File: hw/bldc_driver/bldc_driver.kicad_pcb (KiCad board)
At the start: 2 copper layers, 13 parts, among them Q1 Q_NMOS_DGS, U1 CH32V30xRxTx, U2 STGAP2SCM, U3 STGAP2SCM, U4 STGAP2SCM, U5 STGAP2SCM, U6 STGAP2SCM, U7 STGAP2SCM

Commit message: feat: add CNCs
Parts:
- added C11: 0.1 µF, Capacitor_SMD:C_0805_2012Metric_Pad1.18x1.45mm_HandSolder, F.Cu at (114.5, 88.9)
- added C13: 0.1 µF, Capacitor_SMD:C_0805_2012Metric_Pad1.18x1.45mm_HandSolder, F.Cu at (114.5, 91.9)
- added C15: 0.1 µF, Capacitor_SMD:C_0805_2012Metric_Pad1.18x1.45mm_HandSolder, F.Cu at (114.5, 94.9)
- added C16: 10 µF, Capacitor_SMD:C_0805_2012Metric_Pad1.18x1.45mm_HandSolder, F.Cu at (114.5, 97.9)
- added C17: 0.1 µF, Capacitor_SMD:C_0805_2012Metric_Pad1.18x1.45mm_HandSolder, F.Cu at (114.5, 100.9)
- added C18: 0.1 µF, Capacitor_SMD:C_0805_2012Metric_Pad1.18x1.45mm_HandSolder, F.Cu at (114.5, 103.9)
- added C19: 22 µF, Capacitor_SMD:C_0805_2012Metric_Pad1.18x1.45mm_HandSolder, F.Cu at (114.5, 107.0)
- added C20: 22 µF, Capacitor_SMD:C_0805_2012Metric_Pad1.18x1.45mm_HandSolder, F.Cu at (114.5, 110.0)
- added C21: 0.1 µF, Capacitor_SMD:C_0805_2012Metric_Pad1.18x1.45mm_HandSolder, F.Cu at (119.3, 88.9)
- added C22: 0.1 µF, Capacitor_SMD:C_0805_2012Metric_Pad1.18x1.45mm_HandSolder, F.Cu at (119.3, 91.9)
- added C23: 330 pF, Capacitor_SMD:C_0805_2012Metric_Pad1.18x1.45mm_HandSolder, F.Cu at (119.3, 94.9)
- added C24: 330 pF, Capacitor_SMD:C_0805_2012Metric_Pad1.18x1.45mm_HandSolder, F.Cu at (119.3, 97.9)
- added C25: 0.1 µF, Capacitor_SMD:C_0805_2012Metric_Pad1.18x1.45mm_HandSolder, F.Cu at (119.3, 100.9)
- added C26: 0.1 µF, Capacitor_SMD:C_0805_2012Metric_Pad1.18x1.45mm_HandSolder, F.Cu at (119.3, 103.9)
- added C27: 330 pF, Capacitor_SMD:C_0805_2012Metric_Pad1.18x1.45mm_HandSolder, F.Cu at (119.3, 107.0)
- added C28: 0.1 µF, Capacitor_SMD:C_0805_2012Metric_Pad1.18x1.45mm_HandSolder, F.Cu at (119.3, 110.0)
- added C29: 0.1 µF, Capacitor_SMD:C_0805_2012Metric_Pad1.18x1.45mm_HandSolder, F.Cu at (124.2, 88.9)
- added C30: 330 pF, Capacitor_SMD:C_0805_2012Metric_Pad1.18x1.45mm_HandSolder, F.Cu at (124.2, 91.9)
- added C31: 0.1 µF, Capacitor_SMD:C_0805_2012Metric_Pad1.18x1.45mm_HandSolder, F.Cu at (124.2, 94.9)
- added C32: 0.1 µF, Capacitor_SMD:C_0805_2012Metric_Pad1.18x1.45mm_HandSolder, F.Cu at (124.2, 97.9)
- added C34: 0.1 µF, Capacitor_SMD:C_0805_2012Metric_Pad1.18x1.45mm_HandSolder, F.Cu at (124.2, 100.9)
- added C36: 0.1 µF, Capacitor_SMD:C_0805_2012Metric_Pad1.18x1.45mm_HandSolder, F.Cu at (124.2, 103.9)
- added C38: 0.1 µF, Capacitor_SMD:C_0805_2012Metric_Pad1.18x1.45mm_HandSolder, F.Cu at (124.2, 107.0)
- added C39: 0.1 µF, Capacitor_SMD:C_0805_2012Metric_Pad1.18x1.45mm_HandSolder, F.Cu at (177.0, 96.0)
- added C44: 0.1 µF, Capacitor_SMD:C_0805_2012Metric_Pad1.18x1.45mm_HandSolder, F.Cu at (124.2, 110.0)
- added C46: 0.1 µF, Capacitor_SMD:C_0805_2012Metric_Pad1.18x1.45mm_HandSolder, F.Cu at (129.0, 88.9)
- added C48: 0.1 µF, Capacitor_SMD:C_0805_2012Metric_Pad1.18x1.45mm_HandSolder, F.Cu at (129.0, 91.9)
- added C5: 10 µF, Capacitor_SMD:C_0805_2012Metric_Pad1.18x1.45mm_HandSolder, F.Cu at (177.0, 80.9)
- added C50: 0.1 µF, Capacitor_SMD:C_0805_2012Metric_Pad1.18x1.45mm_HandSolder, F.Cu at (129.0, 94.9)
- added C52: 0.1 µF, Capacitor_SMD:C_0805_2012Metric_Pad1.18x1.45mm_HandSolder, F.Cu at (129.0, 97.9)
- added C54: 0.1 µF, Capacitor_SMD:C_0805_2012Metric_Pad1.18x1.45mm_HandSolder, F.Cu at (129.0, 100.9)
- added C6: 0.1 µF, Capacitor_SMD:C_0805_2012Metric_Pad1.18x1.45mm_HandSolder, F.Cu at (177.0, 83.9)
- added C7: 0.1 µF, Capacitor_SMD:C_0805_2012Metric_Pad1.18x1.45mm_HandSolder, F.Cu at (177.0, 87.0)
- added C8: 22 µF, Capacitor_SMD:C_0805_2012Metric_Pad1.18x1.45mm_HandSolder, F.Cu at (177.0, 90.0)
- added C9: 22 µF, Capacitor_SMD:C_0805_2012Metric_Pad1.18x1.45mm_HandSolder, F.Cu at (177.0, 93.0)
- added D1: KT-0603W, LED_SMD:LED_0603_1608Metric_Pad1.05x0.95mm_HandSolder, F.Cu at (171.7, 92.8)
- added D10: 1N4148WS, Diode_SMD:D_SOD-323_HandSoldering, F.Cu at (151.3, 91.8)
- added D11: 1N4148WS, Diode_SMD:D_SOD-323_HandSoldering, F.Cu at (151.3, 94.8)
- added D12: 1N4148WS, Diode_SMD:D_SOD-323_HandSoldering, F.Cu at (151.3, 97.7)
- added D13: 1N4148WS, Diode_SMD:D_SOD-323_HandSoldering, F.Cu at (151.3, 100.7)
- added D14: 1N4148WS, Diode_SMD:D_SOD-323_HandSoldering, F.Cu at (151.3, 103.6)
- added D15: KT-0603W, LED_SMD:LED_0603_1608Metric_Pad1.05x0.95mm_HandSolder, F.Cu at (171.7, 95.4)
- added D16: KT-0603W, LED_SMD:LED_0603_1608Metric_Pad1.05x0.95mm_HandSolder, F.Cu at (171.7, 98.0)
- added D17: KT-0603W, LED_SMD:LED_0603_1608Metric_Pad1.05x0.95mm_HandSolder, F.Cu at (171.7, 100.6)
- added D2: PESD15VL1BA, Diode_SMD:D_SOD-323_HandSoldering, F.Cu at (187.3, 77.5)
- added D3: MBR20100DT, Package_TO_SOT_SMD:TO-252-2, F.Cu at (92.9, 91.6)
- added D4: MBR20100DT, Package_TO_SOT_SMD:TO-252-2, F.Cu at (92.9, 99.8)
- added D5: MBR20100DT, Package_TO_SOT_SMD:TO-252-2, F.Cu at (92.9, 108.0)
- added D6: MBR20100DT, Package_TO_SOT_SMD:TO-252-2, F.Cu at (92.9, 116.1)
- added D7: MBR20100DT, Package_TO_SOT_SMD:TO-252-2, F.Cu at (92.9, 124.3)
- added D8: MBR20100DT, Package_TO_SOT_SMD:TO-252-2, F.Cu at (92.9, 132.5)
- added D9: 1N4148WS, Diode_SMD:D_SOD-323_HandSoldering, F.Cu at (151.3, 88.9)
- added FL1: BNX025, Filter:Filter_Murata_BNX025, F.Cu at (166.8, 72.4)
- added J1: 430450412, Connector_Molex:Molex_Micro-Fit_3.0_43045-0412_2x02_P3.00mm_Vertical, F.Cu at (161.9, 95.0)
- added J2: B4B-EH-A(LF)(SN), Connector_JST:JST_EH_B4B-EH-A_1x04_P2.50mm_Vertical, F.Cu at (179.8, 68.0)
- added J4: 1733583, TerminalBlock_Phoenix:TerminalBlock_Phoenix_MKDS-1,5-3-5.08_1x03_P5.08mm_Horizontal, F.Cu at (160.8, 85.7)
- added L1: KOHER_MDA7030 15uH, Inductor_SMD:L_KOHERelec_MDA7030, F.Cu at (184.2, 97.5)
- added L2: KOHER_MDA7030 15uH, Inductor_SMD:L_KOHERelec_MDA7030, F.Cu at (116.9, 115.6)
- added Q1: IRF540N, Package_TO_SOT_THT:TO-220-3_Horizontal_TabDown, F.Cu at (89.2, 85.6)
- added Q2: IRF540N, Package_TO_SOT_THT:TO-220-3_Horizontal_TabDown, F.Cu at (100.8, 85.6)
- added Q3: IRF540N, Package_TO_SOT_THT:TO-220-3_Horizontal_TabDown, F.Cu at (112.3, 85.6)
- added Q4: IRF540N, Package_TO_SOT_THT:TO-220-3_Horizontal_TabDown, F.Cu at (123.8, 85.6)
- added Q5: IRF540N, Package_TO_SOT_THT:TO-220-3_Horizontal_TabDown, F.Cu at (135.4, 85.6)
- added Q6: IRF540N, Package_TO_SOT_THT:TO-220-3_Horizontal_TabDown, F.Cu at (146.9, 85.6)
- added R10: 12 ohm, Resistor_SMD:R_0603_1608Metric_Pad0.98x0.95mm_HandSolder, F.Cu at (133.5, 93.7)
- added R11: 12 ohm, Resistor_SMD:R_0603_1608Metric_Pad0.98x0.95mm_HandSolder, F.Cu at (133.5, 96.2)
- added R12: 12 ohm, Resistor_SMD:R_0603_1608Metric_Pad0.98x0.95mm_HandSolder, F.Cu at (133.5, 98.7)
- added R13: 12 ohm, Resistor_SMD:R_0603_1608Metric_Pad0.98x0.95mm_HandSolder, F.Cu at (133.5, 101.2)
- added R14: 12 ohm, Resistor_SMD:R_0603_1608Metric_Pad0.98x0.95mm_HandSolder, F.Cu at (133.5, 103.7)
- added R15: 12 ohm, Resistor_SMD:R_0603_1608Metric_Pad0.98x0.95mm_HandSolder, F.Cu at (133.5, 106.2)
- added R16: 12 ohm, Resistor_SMD:R_0603_1608Metric_Pad0.98x0.95mm_HandSolder, F.Cu at (137.9, 88.6)
- added R17: 12 ohm, Resistor_SMD:R_0603_1608Metric_Pad0.98x0.95mm_HandSolder, F.Cu at (137.9, 91.2)
- added R18: 470 kohm, Resistor_SMD:R_0603_1608Metric_Pad0.98x0.95mm_HandSolder, F.Cu at (137.9, 93.7)
- added R19: 10 kohm, Resistor_SMD:R_0603_1608Metric_Pad0.98x0.95mm_HandSolder, F.Cu at (137.9, 96.2)
- added R2: 100 Ohm, Resistor_SMD:R_0603_1608Metric_Pad0.98x0.95mm_HandSolder, F.Cu at (186.2, 80.7)
- added R20: 470 kohm, Resistor_SMD:R_0603_1608Metric_Pad0.98x0.95mm_HandSolder, F.Cu at (137.9, 98.7)
- added R21: 10 kohm, Resistor_SMD:R_0603_1608Metric_Pad0.98x0.95mm_HandSolder, F.Cu at (137.9, 101.2)
- added R22: 470 kohm, Resistor_SMD:R_0603_1608Metric_Pad0.98x0.95mm_HandSolder, F.Cu at (137.9, 103.7)
- added R23: 10 kohm, Resistor_SMD:R_0603_1608Metric_Pad0.98x0.95mm_HandSolder, F.Cu at (137.9, 106.2)
- added R24: 12 ohm, Resistor_SMD:R_0603_1608Metric_Pad0.98x0.95mm_HandSolder, F.Cu at (142.2, 88.6)
- added R25: 12 ohm, Resistor_SMD:R_0603_1608Metric_Pad0.98x0.95mm_HandSolder, F.Cu at (142.2, 91.2)
- added R26: 12 ohm, Resistor_SMD:R_0603_1608Metric_Pad0.98x0.95mm_HandSolder, F.Cu at (142.2, 93.7)
- added R27: 12 ohm, Resistor_SMD:R_0603_1608Metric_Pad0.98x0.95mm_HandSolder, F.Cu at (142.2, 96.2)
- added R28: 12 ohm, Resistor_SMD:R_0603_1608Metric_Pad0.98x0.95mm_HandSolder, F.Cu at (142.2, 98.7)
- added R29: 12 ohm, Resistor_SMD:R_0603_1608Metric_Pad0.98x0.95mm_HandSolder, F.Cu at (142.2, 101.2)
- added R3: 0 ohm, Resistor_SMD:R_0201_0603Metric_Pad0.64x0.40mm_HandSolder, F.Cu at (176.0, 98.4)
- added R30: 12 ohm, Resistor_SMD:R_0603_1608Metric_Pad0.98x0.95mm_HandSolder, F.Cu at (142.2, 103.7)
- added R31: 12 ohm, Resistor_SMD:R_0603_1608Metric_Pad0.98x0.95mm_HandSolder, F.Cu at (142.2, 106.2)
- added R32: 12 ohm, Resistor_SMD:R_0603_1608Metric_Pad0.98x0.95mm_HandSolder, F.Cu at (146.6, 88.6)
- added R33: 12 ohm, Resistor_SMD:R_0603_1608Metric_Pad0.98x0.95mm_HandSolder, F.Cu at (146.6, 91.2)
- added R34: 12 ohm, Resistor_SMD:R_0603_1608Metric_Pad0.98x0.95mm_HandSolder, F.Cu at (146.6, 93.7)
- added R35: 12 ohm, Resistor_SMD:R_0603_1608Metric_Pad0.98x0.95mm_HandSolder, F.Cu at (146.6, 96.2)
- added R36: 100 Ohm, Resistor_SMD:R_0603_1608Metric_Pad0.98x0.95mm_HandSolder, F.Cu at (186.2, 88.2)
- added R37: 100 Ohm, Resistor_SMD:R_0603_1608Metric_Pad0.98x0.95mm_HandSolder, F.Cu at (186.2, 90.7)
- added R4: 100 kohm, Resistor_SMD:R_0201_0603Metric_Pad0.64x0.40mm_HandSolder, F.Cu at (176.0, 100.1)
- added R5: 22 kohm, Resistor_SMD:R_0603_1608Metric_Pad0.98x0.95mm_HandSolder, F.Cu at (186.2, 83.2)
- added R6: 100 Ohm, Resistor_SMD:R_0603_1608Metric_Pad0.98x0.95mm_HandSolder, F.Cu at (186.2, 85.7)
- added R7: 0 ohm, Resistor_SMD:R_0201_0603Metric_Pad0.64x0.40mm_HandSolder, F.Cu at (113.5, 134.7)
- added R8: 200 kohm, Resistor_SMD:R_0603_1608Metric_Pad0.98x0.95mm_HandSolder, F.Cu at (133.5, 88.6)
- added R9: 27 kohm, Resistor_SMD:R_0603_1608Metric_Pad0.98x0.95mm_HandSolder, F.Cu at (133.5, 91.2)
- added TP1: TestPoint_Flag, TestPoint:TestPoint_Plated_Hole_D2.0mm, F.Cu at (181.7, 81.8)
- added TP2: TestPoint_Flag, TestPoint:TestPoint_Plated_Hole_D2.0mm, F.Cu at (181.7, 86.4)
- added TP3: TestPoint_Flag, TestPoint:TestPoint_Plated_Hole_D2.0mm, F.Cu at (181.7, 91.1)
- added TP4: TestPoint_Flag, TestPoint:TestPoint_Plated_Hole_D2.0mm, F.Cu at (114.5, 122.0)
- added TP5: TestPoint_Flag, TestPoint:TestPoint_Plated_Hole_D2.0mm, F.Cu at (114.5, 126.7)
- added U10: TPS54202DDC, Package_TO_SOT_SMD:SOT-23-6_Handsoldering, F.Cu at (115.0, 131.5)
- added U11: AMC1200BDWV, Package_SO:SOIC-8_7.5x5.85mm_P1.27mm, F.Cu at (105.1, 98.5)
- added U12: AMC1200BDWV, Package_SO:SOIC-8_7.5x5.85mm_P1.27mm, F.Cu at (105.1, 105.9)
- added U13: AMC1200BDWV, Package_SO:SOIC-8_7.5x5.85mm_P1.27mm, F.Cu at (105.1, 113.3)
- added U14: SN65HVD230, Package_SO:SOIC-8_3.9x4.9mm_P1.27mm, F.Cu at (180.5, 74.6)
- added U8: TPS54202DDC, Package_TO_SOT_SMD:SOT-23-6_Handsoldering, F.Cu at (187.7, 73.7)
- added U9: AMC1200BDWV, Package_SO:SOIC-8_7.5x5.85mm_P1.27mm, F.Cu at (105.1, 91.1)
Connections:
- U1 pad 10: /Motor/PH_V_HI -> /Motor/W_ADC_P
- U1 pad 11: /Motor/PH_V_LO -> /Motor/SHUNT_CURR_P
- U1 pad 24: /Motor/PH_W_HI -> unconnected-(U1-PC4-Pad24)
- U1 pad 25: /Motor/PH_W_LO -> unconnected-(U1-PC5-Pad25)
- U1 pad 34: unconnected-(U1-PB13-Pad34) -> Net-(D15-A)
- U1 pad 35: unconnected-(U1-PB14-Pad35) -> Net-(D16-A)
- U1 pad 36: unconnected-(U1-PB15-Pad36) -> Net-(D17-A)
- U1 pad 37: unconnected-(U1-PC6-Pad37) -> /Motor/PH_U_HI
- U1 pad 38: unconnected-(U1-PC7-Pad38) -> /Motor/PH_U_LO
- U1 pad 39: unconnected-(U1-PC8-Pad39) -> /Motor/PH_V_HI
- U1 pad 40: unconnected-(U1-PC9-Pad40) -> /Motor/PH_V_LO
- U1 pad 44: unconnected-(U1-PA11-Pad44) -> /CAN_RX
- U1 pad 45: unconnected-(U1-PA12-Pad45) -> /CAN_TX
- U1 pad 46: unconnected-(U1-SWDIO-Pad46) -> Net-(J2-Pin_3)
- U1 pad 49: unconnected-(U1-SWCLK-Pad49) -> Net-(J2-Pin_2)
- U1 pad 51: unconnected-(U1-PC10-Pad51) -> /Motor/PH_W_HI
- U1 pad 52: unconnected-(U1-PC11-Pad52) -> /Motor/PH_W_LO
- U1 pad 8: /Motor/PH_U_HI -> /Motor/U_ADC_P
- U1 pad 9: /Motor/PH_U_LO -> /Motor/V_ADC_P
- U2 pad 1: unconnected-(U2-VDD-Pad1) -> +3V3
- U2 pad 4: unconnected-(U2-GND-Pad4) -> GND
- U2 pad 5: unconnected-(U2-VH-Pad5) -> +VDC
- U2 pad 6: unconnected-(U2-GOUT-Pad6) -> Net-(D9-K)
- U2 pad 7: unconnected-(U2-CLAMP-Pad7) -> Net-(Q2-G)
- U2 pad 8: unconnected-(U2-GNDISO-Pad8) -> GNDPWR
- U3 pad 1: unconnected-(U3-VDD-Pad1) -> +3V3
- U3 pad 4: unconnected-(U3-GND-Pad4) -> GND
- U3 pad 5: unconnected-(U3-VH-Pad5) -> +VDC
- U3 pad 6: unconnected-(U3-GOUT-Pad6) -> Net-(D10-K)
- U3 pad 7: unconnected-(U3-CLAMP-Pad7) -> Net-(Q1-G)
- U3 pad 8: unconnected-(U3-GNDISO-Pad8) -> GNDPWR
- U4 pad 1: unconnected-(U4-VDD-Pad1) -> +3V3
- U4 pad 4: unconnected-(U4-GND-Pad4) -> GND
- U4 pad 5: unconnected-(U4-VH-Pad5) -> +VDC
- U4 pad 6: unconnected-(U4-GOUT-Pad6) -> Net-(D11-K)
- U4 pad 7: unconnected-(U4-CLAMP-Pad7) -> Net-(Q3-G)
- U4 pad 8: unconnected-(U4-GNDISO-Pad8) -> GNDPWR
- U5 pad 1: unconnected-(U5-VDD-Pad1) -> +3V3
- U5 pad 4: unconnected-(U5-GND-Pad4) -> GND
- U5 pad 5: unconnected-(U5-VH-Pad5) -> +VDC
- U5 pad 6: unconnected-(U5-GOUT-Pad6) -> Net-(D12-K)
- U5 pad 7: unconnected-(U5-CLAMP-Pad7) -> Net-(Q4-G)
- U5 pad 8: unconnected-(U5-GNDISO-Pad8) -> GNDPWR
- U6 pad 1: unconnected-(U6-VDD-Pad1) -> +3V3
- U6 pad 4: unconnected-(U6-GND-Pad4) -> GND
- U6 pad 5: unconnected-(U6-VH-Pad5) -> +VDC
- U6 pad 6: unconnected-(U6-GOUT-Pad6) -> Net-(D13-K)
- U6 pad 7: unconnected-(U6-CLAMP-Pad7) -> Net-(Q5-G)
- U6 pad 8: unconnected-(U6-GNDISO-Pad8) -> GNDPWR
- U7 pad 1: unconnected-(U7-VDD-Pad1) -> +3V3
- U7 pad 4: unconnected-(U7-GND-Pad4) -> GND
- U7 pad 5: unconnected-(U7-VH-Pad5) -> +VDC
- U7 pad 6: unconnected-(U7-GOUT-Pad6) -> Net-(D14-K)
- U7 pad 7: unconnected-(U7-CLAMP-Pad7) -> Net-(Q6-G)
- U7 pad 8: unconnected-(U7-GNDISO-Pad8) -> GNDPWR
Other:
- board outline added: 127.5 x 96 mm

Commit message: feat: start PCB
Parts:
- added F1: BSMD1206C-2200T, Fuse:Fuse_1206_3216Metric_Pad1.42x1.75mm_HandSolder, F.Cu at (155.9, 123.9)
- added J3: B4B-EH-A(LF)(SN), Connector_JST:JST_EH_B4B-EH-A_1x04_P2.50mm_Vertical, F.Cu at (156.5, 119.0)
- added TP6: TestPoint_Flag, TestPoint:TestPoint_Plated_Hole_D2.0mm, F.Cu at (150.7, 118.7)
- added TP7: TestPoint_Flag, TestPoint:TestPoint_Plated_Hole_D2.0mm, F.Cu at (150.7, 123.3)
- added TP8: TestPoint_Flag, TestPoint:TestPoint_Plated_Hole_D2.0mm, F.Cu at (150.7, 128.0)
- added TP9: TestPoint_Flag, TestPoint:TestPoint_Plated_Hole_D2.0mm, F.Cu at (150.7, 132.7)
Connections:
- J1 pad 1: +VDC -> Net-(J1-Pin_1)
- U1 pad 29: unconnected-(U1-PB10-Pad29) -> /USART3_TX
- U1 pad 30: unconnected-(U1-PB11-Pad30) -> /USART3_RX

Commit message: bldc: start placement
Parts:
- removed Q1: Q_NMOS_DGS, Package_TO_SOT_SMD:TO-252-2
- removed Q1: IRF540N, Package_TO_SOT_THT:TO-220-3_Horizontal_TabDown
- removed TP4: TestPoint_Flag, TestPoint:TestPoint_Plated_Hole_D2.0mm
- added C10: 1 µF, Capacitor_SMD:C_0805_2012Metric_Pad1.18x1.45mm_HandSolder, F.Cu at (139.7, 79.2)
- added C12: 1 µF, Capacitor_SMD:C_0805_2012Metric_Pad1.18x1.45mm_HandSolder, F.Cu at (89.0, 64.0)
- added C14: 1 µF, Capacitor_SMD:C_0805_2012Metric_Pad1.18x1.45mm_HandSolder, F.Cu at (89.0, 67.1)
- added C33: 1 µF, Capacitor_SMD:C_0805_2012Metric_Pad1.18x1.45mm_HandSolder, F.Cu at (89.0, 70.1)
- added C35: 1 µF, Capacitor_SMD:C_0805_2012Metric_Pad1.18x1.45mm_HandSolder, F.Cu at (93.8, 61.0)
- added C37: 1 µF, Capacitor_SMD:C_0805_2012Metric_Pad1.18x1.45mm_HandSolder, F.Cu at (93.8, 64.0)
- added C43: 1 µF, Capacitor_SMD:C_0805_2012Metric_Pad1.18x1.45mm_HandSolder, F.Cu at (93.8, 67.1)
- added C45: 1 µF, Capacitor_SMD:C_0805_2012Metric_Pad1.18x1.45mm_HandSolder, F.Cu at (93.8, 70.1)
- added C47: 1 µF, Capacitor_SMD:C_0805_2012Metric_Pad1.18x1.45mm_HandSolder, F.Cu at (98.6, 61.0)
- added C49: 1 µF, Capacitor_SMD:C_0805_2012Metric_Pad1.18x1.45mm_HandSolder, F.Cu at (98.6, 64.0)
- added C51: 1 µF, Capacitor_SMD:C_0805_2012Metric_Pad1.18x1.45mm_HandSolder, F.Cu at (98.6, 67.1)
- added C53: 1 µF, Capacitor_SMD:C_0805_2012Metric_Pad1.18x1.45mm_HandSolder, F.Cu at (98.6, 70.1)
- added Q7: IRF540N, Package_TO_SOT_THT:TO-220-3_Horizontal_TabDown, F.Cu at (109.3, 99.5)
- added Rshunt1: HoLLR2512-3W-15mR-1%, Resistor_SMD:R_2512_6332Metric_Pad1.40x3.35mm_HandSolder, B.Cu at (124.2, 96.6)
- C1, C11, C13, C15, C16, C17, C18, C2, C21, C22, C23, C24, C25, C26, C27, C28, C29, C3, C30, C31, C32, C34, C36, C38, C4, C44, C46, C48, C50, C52, C54, C6, C7, D3, D4, D5, D6, D7, D8, R10, R11, R12, R13, R14, R15, R16, R17, R18, R19, R20, R21, R22, R23, R24, R25, R26, R27, R28, R29, R30, R31, R32, R34, R35, R5, R9, U11, U9: moved to B.Cu
- moved TP9 93.0 mm to (73.5, 80.6), turned to 180 degrees
- moved TP8 87.3 mm to (77.3, 80.6)
- moved J4 83.3 mm to (77.5, 85.9), turned to -90 degrees
- moved TP7 81.7 mm to (81.0, 80.6)
- moved R35 76.1 mm to (79.5, 60.2), turned to 90 degrees
- moved R31 75.4 mm to (78.3, 66.3), turned to 90 degrees
- moved R34 72.7 mm to (82.0, 60.2), turned to 90 degrees
- moved R30 71.9 mm to (80.8, 66.3), turned to 90 degrees
- moved R23 69.4 mm to (78.3, 70.6), turned to 90 degrees
- moved R29 68.5 mm to (83.3, 66.3), turned to 90 degrees
- moved R32 67.6 mm to (85.3, 60.1), turned to 90 degrees
- moved R22 66.0 mm to (80.8, 70.6), turned to 90 degrees
- moved R28 65.0 mm to (85.9, 66.3), turned to 90 degrees
- moved U2 63.9 mm to (133.0, 82.6), turned to 180 degrees
- moved U4 62.9 mm to (133.0, 93.8), turned to 180 degrees
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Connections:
- net Net-(J2-Pin_2) renamed /SWCLK
- net Net-(J2-Pin_3) renamed /SWDIO
- J4 pad 1: /Motor/MOTOR_U -> /Motor/MOTOR_W
- J4 pad 3: /Motor/MOTOR_W -> /Motor/MOTOR_U
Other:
- board size 127.5 x 96 mm -> 101 x 48 mm
- copper layers 2 -> 4
- board text added: "+3V3"
- board text added: "CAN_H"
- board text added: "CAN_L"
- board text added: "FUSE"
- board text added: "GND"
- board text added: "GNDPWR"
- board text added: "PGOOD 3V3"
- board text added: "POWER"
- board text added: "RX"
- board text added: "SWCLK"
- board text added: "SWDIO"
- board text added: "TX"
- board text added: "U"
- board text added: "V"
- board text added: "W"

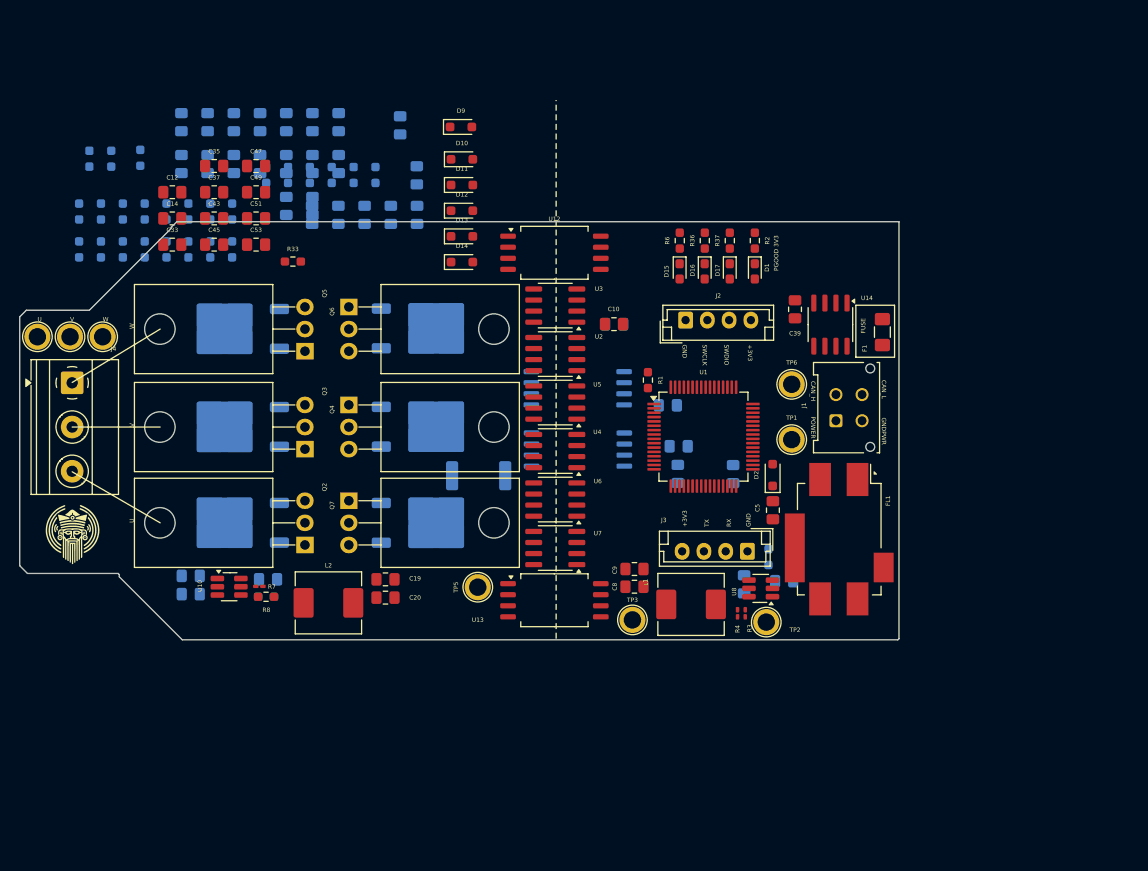
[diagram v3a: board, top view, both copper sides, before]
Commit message: bldc: placement mostly done
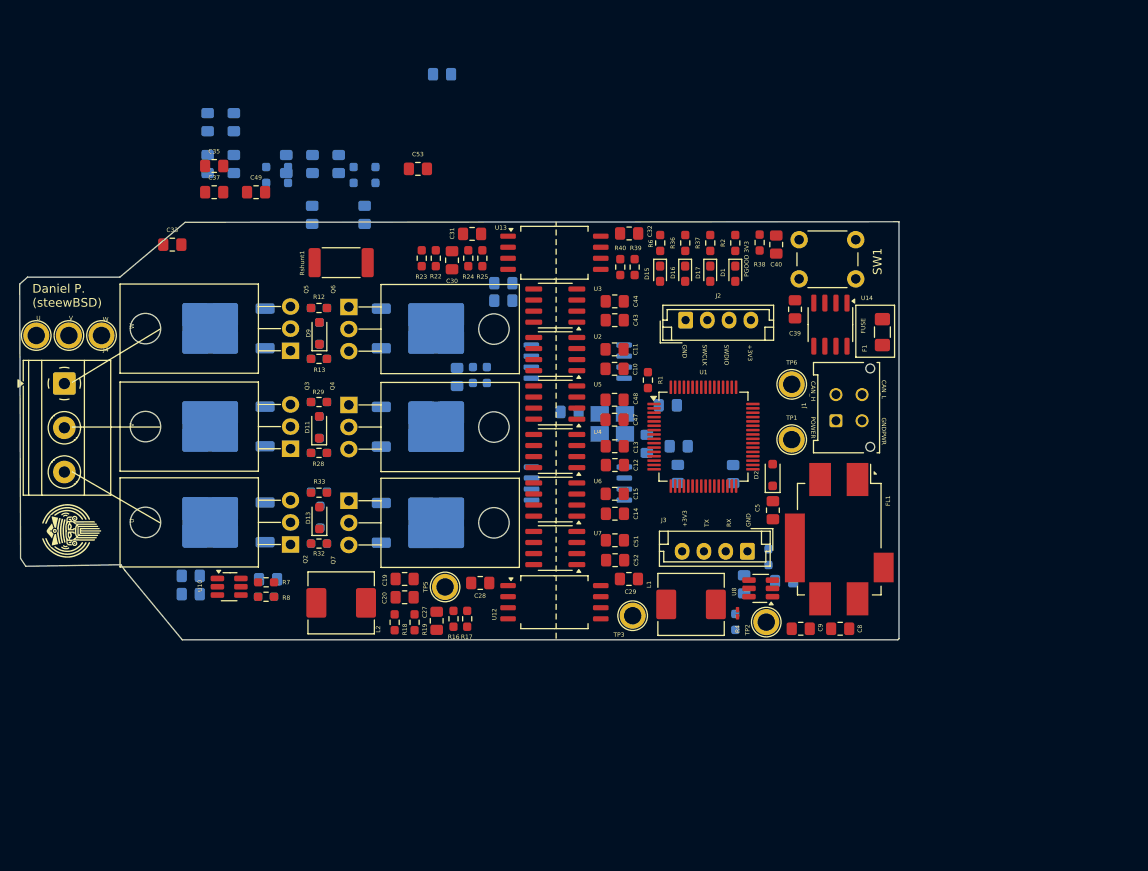
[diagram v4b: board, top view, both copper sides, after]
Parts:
- added C40: 0.1 µF, Capacitor_SMD:C_0805_2012Metric_Pad1.18x1.45mm_HandSolder, F.Cu at (158.4, 70.1)
- added C41: 10 pF, Capacitor_SMD:C_0805_2012Metric_Pad1.18x1.45mm_HandSolder, B.Cu at (134.6, 89.3)
- added C42: 10 pF, Capacitor_SMD:C_0805_2012Metric_Pad1.18x1.45mm_HandSolder, B.Cu at (143.5, 92.9)
- added R38: 4.7 kohm, Resistor_SMD:R_0603_1608Metric_Pad0.98x0.95mm_HandSolder, F.Cu at (156.5, 69.8)
- added R39: 4.7 kohm, Resistor_SMD:R_0603_1608Metric_Pad0.98x0.95mm_HandSolder, F.Cu at (142.1, 72.6)
- added R40: 4.7 kohm, Resistor_SMD:R_0603_1608Metric_Pad0.98x0.95mm_HandSolder, F.Cu at (140.5, 72.6)
- added SW1: BTSA-N-P-1, Button_Switch_THT:SW_PUSH_6mm_H8mm, F.Cu at (161.0, 69.5)
- added Y1: Crystal_GND24, Crystal:Crystal_SMD_3225-4Pin_3.2x2.5mm_HandSoldering, B.Cu at (139.6, 90.7)
- C11, C13, C15, C27, C28, C29, C30, C31, C32, C44, C48, C52, R12, R13, R16, R17, R18, R19, R22, R23, R24, R25, R28, R29, R32, Rshunt1: moved to F.Cu
- C45, D10, D12, D14: moved to B.Cu
- R3: footprint Resistor_SMD:R_0201_0603Metric_Pad0.64x0.40mm_HandSolder -> Resistor_SMD:R_0603_1608Metric_Pad0.98x0.95mm_HandSolder; moved to B.Cu
- R7: footprint Resistor_SMD:R_0201_0603Metric_Pad0.64x0.40mm_HandSolder -> Resistor_SMD:R_0603_1608Metric_Pad0.98x0.95mm_HandSolder
- moved C29 62.1 mm to (141.5, 108.5), turned to 180 degrees
- moved C14 61.1 mm to (139.8, 101.0)
- moved C27 60.1 mm to (119.4, 113.3), turned to -90 degrees
- moved C12 59.7 mm to (139.8, 95.4)
- moved C51 55.4 mm to (139.8, 104.0)
- moved C28 53.3 mm to (124.4, 108.9), turned to 0 degrees
- moved R17 51.7 mm to (122.9, 113.0)
- moved R19 51.4 mm to (116.8, 113.4), turned to -90 degrees
- moved C52 50.8 mm to (139.9, 106.3), turned to 0 degrees
- moved C47 50.4 mm to (139.8, 90.2)
- moved R34 50.2 mm to (105.9, 104.4), turned to 0 degrees
- moved C15 50.2 mm to (139.8, 98.7), turned to 0 degrees
- moved R16 49.5 mm to (121.3, 113.0)
- moved R18 48.9 mm to (114.6, 113.4)
- moved R32 48.8 mm to (105.9, 104.4), turned to 180 degrees
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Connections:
- U1 pad 5: unconnected-(U1-OSC_IN-Pad5) -> Net-(U1-OSC_IN)
- U1 pad 6: unconnected-(U1-OSC_OUT-Pad6) -> Net-(U1-OSC_OUT)
- U1 pad 60: unconnected-(U1-BOOT0-Pad60) -> Net-(U1-BOOT0)
- U1 pad 7: unconnected-(U1-~{RST}-Pad7) -> Net-(U1-~{RST})
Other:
- outline, holes or cut-outs redrawn
- board text added: "Daniel P. (steewBSD)"
- board text added: "RESET"

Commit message: bldc: finish placement
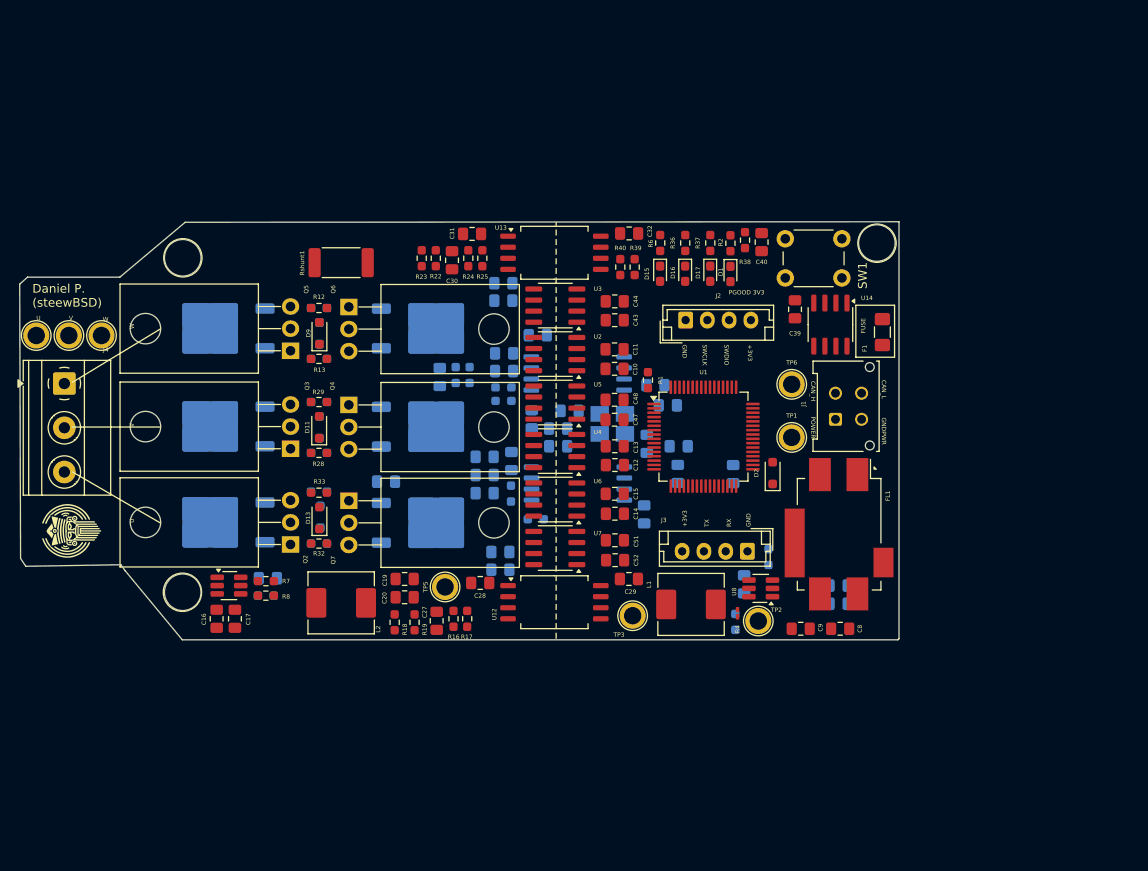
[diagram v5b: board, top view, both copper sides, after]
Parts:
- C16, C17: moved to F.Cu
- C33, C35, C37, C49, C5, C53: moved to B.Cu
- moved C26 57.3 mm to (144.5, 86.2), turned to 180 degrees
- moved C22 55.4 mm to (143.2, 101.0)
- moved C36 52.3 mm to (128.0, 94.9), turned to -90 degrees
- moved C35 49.7 mm to (133.3, 91.2)
- moved C37 46.5 mm to (124.9, 98.6), turned to 180 degrees
- moved C38 46.3 mm to (124.9, 96.5)
- moved C54 46.1 mm to (126.7, 107.4), turned to 180 degrees
- moved C53 45.0 mm to (126.7, 105.4), turned to 180 degrees
- moved R11 44.7 mm to (130.8, 101.6), turned to 180 degrees
- moved C34 42.2 mm to (127.1, 84.6), turned to 180 degrees
- moved C21 41.1 mm to (133.3, 93.2), turned to 180 degrees
- moved C49 40.2 mm to (124.9, 94.4), turned to 180 degrees
- moved C33 40.1 mm to (127.1, 82.5), turned to 180 degrees
- moved C25 40.1 mm to (131.0, 80.5), turned to 180 degrees
- moved R10 39.8 mm to (127.9, 98.7)
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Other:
- outline, holes or cut-outs redrawn

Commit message: bldc: pre-routing commit
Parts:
- moved TP5 43.4 mm to (100.5, 70.8)
- moved L2 32.0 mm to (77.2, 104.3)
- moved C16 14.9 mm to (109.0, 112.3)
- moved C17 14.9 mm to (111.1, 112.3)
- moved R25 10.0 mm to (114.7, 69.9), turned to -90 degrees
- moved C42 9.65 mm to (153.1, 92.2), turned to 0 degrees
- moved C21 9.08 mm to (136.0, 101.9)
- moved C41 8.85 mm to (143.5, 89.6)
- moved Y1 8.76 mm to (148.3, 90.9)
- moved C18 8.34 mm to (107.3, 112.3), turned to 90 degrees
- moved R8 7.63 mm to (107.1, 112.6), turned to -90 degrees
- moved U10 7.46 mm to (102.3, 112.4)
- moved R7 6.94 mm to (105.5, 112.6), turned to -90 degrees
- moved R24 6.88 mm to (116.4, 69.9), turned to -90 degrees
- moved R9 6.18 mm to (105.5, 112.6), turned to 90 degrees
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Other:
- outline, holes or cut-outs redrawn
- board text added: "PG 3V3"
- board text removed: "PGOOD 3V3"

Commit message: bldc: pre branch
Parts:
- moved TP7 0.20 mm to (81.1, 80.6)
- moved TP8 0.20 mm to (77.3, 80.6)
- moved TP9 0.20 mm to (73.6, 80.6)
- turned L2 to 180 degrees
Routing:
- net Net-(U1-OSC_OUT): track 0.00 -> 2.42 mm
- net Net-(U1-OSC_IN): track 0.00 -> 2.40 mm
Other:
- outline, holes or cut-outs redrawn
